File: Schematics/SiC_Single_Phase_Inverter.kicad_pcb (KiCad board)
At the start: 2 copper layers, 200 x 84 mm, 107 parts, among them J1 23AH8785-Black, J2 23AH8786-Red, Q1 STB10NK60ZT4, Q2 STB10NK60ZT4, Q3 C3M0025065K, Q4 C3M0025065K, Q5 C3M0025065K, Q6 C3M0025065K, Q7 C3M0025065K, U1 UCC21710QDWRQ1, U2 UCC21710QDWRQ1, U3 UCC21710QDWRQ1, U4 UCC21710QDWRQ1

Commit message: [WIP SiC Single Phase Inverter
- Updated README.md
- Added New Parts for Output filter L,C,R
- Added datasheets for the new parts
- Added 3D models for the new parts
- Added new symbols and footprints for the L,C,R
- Finished output filter
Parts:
- added C53: 6.8 uF, SiC_Inverter:C4AF9BW4680T3FK, F.Cu at (285.0, 65.0)
- added J3: 23AH8786-Red, SiC_Inverter:23AH8786-Red, F.Cu at (273.3, 74.1)
- added J4: 23AH8785-Black, SiC_Inverter:23AH8785-Black, F.Cu at (273.4, 108.4)
- added L3: 470 uH, SiC_Inverter:1140471KRC, F.Cu at (229.2, 66.4)
- added L4: 470 uH, SiC_Inverter:1140471KRC, F.Cu at (229.2, 107.6)
- added R34: R, SiC_Inverter:CW005100R0JE12HE, F.Cu at (287.6, 78.0)
- moved C1 51.0 mm to (126.6, 84.3)
- moved L2 51.0 mm to (92.0, 70.7)
- moved C12 51.0 mm to (57.4, 53.8)
- moved C13 51.0 mm to (57.4, 64.9)
- moved C14 51.0 mm to (57.4, 76.1)
- moved C15 51.0 mm to (57.4, 87.2)
- moved C16 51.0 mm to (57.4, 98.4)
- moved C17 51.0 mm to (214.4, 79.0)
- moved C18 51.0 mm to (203.7, 102.7)
- moved C19 51.0 mm to (203.7, 105.7)
- moved C2 51.0 mm to (28.9, 55.4)
- moved C20 51.0 mm to (213.4, 102.8)
- moved C21 51.0 mm to (203.7, 108.7)
- moved C22 51.0 mm to (214.4, 82.4)
- moved C23 51.0 mm to (213.4, 106.2)
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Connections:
- net /Input_Protection/Gate_node_Inpro renamed /Input_Protection/Gate_node_input_pro
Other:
- board size 200 x 84 mm -> 318.5 x 84 mm

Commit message: [WIP SiC Single Phase Inverter]
- Added PCB to PCB Male and Female connectors
- Added symbols, footprints and 3d models for the parts listed above
- Added Male and Female connectors to input protection and input emi
  subsheets
- Changed PCB editor to account for two edge cuts/ two sub circuits
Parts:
- removed Q6: C3M0025065K, SiC_Inverter:C3M0025065K
- added J5: 464369202, SiC_Inverter:46436-900_02, F.Cu at (98.3, 42.2)
- added J6: 464379202, SiC_Inverter:46437-900_02, F.Cu at (141.0, 35.0)
- added J7: 464369202, SiC_Inverter:46436-900_02, F.Cu at (237.0, 59.0)
- moved C12 377.7 mm to (434.3, 29.5)
- moved C13 377.7 mm to (434.3, 40.6)
- moved C14 377.7 mm to (434.3, 51.8)
- moved C15 377.7 mm to (434.3, 63.0)
- moved C16 377.7 mm to (434.3, 74.1)
- moved C2 377.7 mm to (405.8, 31.2)
- moved C3 377.7 mm to (405.8, 45.7)
- moved C4 377.7 mm to (405.8, 60.3)
- moved C5 377.7 mm to (405.8, 74.8)
- moved C6 377.7 mm to (405.8, 89.4)
- moved C10 377.7 mm to (420.7, 74.8)
- moved C11 377.7 mm to (420.7, 89.4)
- moved C7 377.7 mm to (420.7, 31.2)
- moved C8 377.7 mm to (420.7, 45.7)
- moved C9 377.7 mm to (420.7, 60.3)
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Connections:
- D1 pad 1: /Input_Protection/Gate_node_input_pro -> GND
- R1 pad 2: /Input_Protection/Gate_node_input_pro -> GND
- R2 pad 2: /Input_Protection/Gate_node_input_pro -> GND
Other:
- board size 318.5 x 84 mm -> 204.5 x 65.2 mm
- board text added: "DC Input and Input Protection Circuit"
- board text added: "EMI Input Filter"

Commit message: [WIP Single Phase SiC Inverter]
- Added molex 4 pin pcb connector for +15V power
- Added 3d model, symbol and footprint
- Added datasheet for molex connector
- Added Male and Female pcb - pcb connectors to all sub sheets
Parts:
- added J10: 464379202, SiC_Inverter:46437-900_02, F.Cu at (397.3, 112.2)
- added J11: 464369202, SiC_Inverter:46436-900_02, F.Cu at (380.2, 112.2)
- added J12: 464379202, SiC_Inverter:46437-900_02, F.Cu at (461.5, 44.5)
- added J13: 464369202, SiC_Inverter:46436-900_02, F.Cu at (461.5, 17.4)
- added J14: 464379202, SiC_Inverter:46437-900_02, F.Cu at (458.6, 111.0)
- added J15: 464369202, SiC_Inverter:46436-900_02, F.Cu at (476.0, 111.0)
- added J16: 464379202, SiC_Inverter:46437-900_02, F.Cu at (349.7, 50.9)
- added J8: 43650-0418, SiC_Inverter:436500418, F.Cu at (356.5, 155.2)
- added J9: 43650-0418, SiC_Inverter:436500418, F.Cu at (467.6, 95.1)
- added PS1: IRM-03-15, SiC_Inverter:IRM-03-15, F.Cu at (323.0, 163.1)
- added PS2: IRM-03-15, SiC_Inverter:IRM-03-15, F.Cu at (323.0, 188.6)
- moved J2 405.5 mm to (435.0, 158.8), turned to 0 degrees
- moved J1 388.3 mm to (421.4, 158.8), turned to 0 degrees
- moved D1 382.4 mm to (423.1, 194.1)
- moved D2 382.4 mm to (416.5, 189.3)
- moved F1 382.4 mm to (432.0, 173.6)
- moved Q1 382.4 mm to (425.3, 180.5)
- moved R1 382.4 mm to (417.5, 193.5)
- moved R2 382.4 mm to (417.5, 196.8)
- moved J5 368.3 mm to (437.4, 186.0), turned to 0 degrees
- moved J6 237.9 mm to (360.9, 125.9), turned to 0 degrees
- moved L2 160.8 mm to (304.8, 112.7)
- moved L1 156.5 mm to (307.3, 131.3)
- moved C1 146.2 mm to (339.6, 102.3)
- moved J7 126.0 mm to (343.8, 125.9), turned to 0 degrees
- moved R3 100.2 mm to (376.9, 95.4)
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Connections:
- C17 pad 2: GND_ISO_LALS -> GND_ISO_LAHS
- C22 pad 1: +15V__ISO_LAHS -> +15V_ISO_LALS
- C26 pad 1: +15V__ISO_LAHS -> +15V_ISO_LALS
- C27 pad 1: +15V__ISO_LAHS -> +15V_ISO_LALS
- C29 pad 2: GND_ISO_LALS -> GND_ISO_LAHS
- C30 pad 2: GND_ISO_LALS -> GND_ISO_LAHS
- C35 pad 1: +15V__ISO_LBHS -> +15V_ISO_LBLS
- C36 pad 2: GND_ISO_LBLS -> GND_ISO_LBHS
- C37 pad 1: +15V__ISO_LBHS -> +15V_ISO_LBLS
- C38 pad 2: GND_ISO_LBLS -> GND_ISO_LBHS
- C39 pad 1: +15V__ISO_LBHS -> +15V_ISO_LBLS
- C40 pad 2: GND_ISO_LBLS -> GND_ISO_LBHS
- D2 pad 1: /Input_Protection/+VIN_Protected -> /EMI_Input_Filter/+VIN_EMI
- D4 pad 2: GND_ISO_LALS -> GND_ISO_LAHS
- D6 pad 2: GND_ISO_LBLS -> GND_ISO_LBHS
- F1 pad 2: /Input_Protection/+VIN_Protected -> /EMI_Input_Filter/+VIN_EMI
- J5 pad P1_1: /Input_Protection/+VIN_Protected -> /EMI_Input_Filter/+VIN_EMI
- J5 pad P1_10: /Input_Protection/+VIN_Protected -> /EMI_Input_Filter/+VIN_EMI
- J5 pad P1_2: /Input_Protection/+VIN_Protected -> /EMI_Input_Filter/+VIN_EMI
- J5 pad P1_3: /Input_Protection/+VIN_Protected -> /EMI_Input_Filter/+VIN_EMI
- J5 pad P1_4: /Input_Protection/+VIN_Protected -> /EMI_Input_Filter/+VIN_EMI
- J5 pad P1_5: /Input_Protection/+VIN_Protected -> /EMI_Input_Filter/+VIN_EMI
- J5 pad P1_6: /Input_Protection/+VIN_Protected -> /EMI_Input_Filter/+VIN_EMI
- J5 pad P1_7: /Input_Protection/+VIN_Protected -> /EMI_Input_Filter/+VIN_EMI
- J5 pad P1_8: /Input_Protection/+VIN_Protected -> /EMI_Input_Filter/+VIN_EMI
- J5 pad P1_9: /Input_Protection/+VIN_Protected -> /EMI_Input_Filter/+VIN_EMI
- Q3 pad 1: /Full-Bridge/BUS_DC+ -> /DC_Link_Caps/BUS_DC+
- Q4 pad 1: /Full-Bridge/BUS_DC+ -> /DC_Link_Caps/BUS_DC+
- Q5 pad 2: GND_ISO_LBLS -> GND_ISO_LBHS
- Q5 pad 3: GND_ISO_LBLS -> GND_ISO_LBHS
- Q7 pad 2: GND_ISO_LALS -> GND_ISO_LAHS
- Q7 pad 3: GND_ISO_LALS -> GND_ISO_LAHS
- R21 pad 2: GND_ISO_LBLS -> GND_ISO_LBHS
- R8 pad 2: GND_ISO_LALS -> GND_ISO_LAHS
- U1 pad 5: +15V__ISO_LAHS -> +15V_ISO_LALS
- U2 pad 1: GND_ISO_LALS -> GND_ISO_LAHS
- U2 pad 2: GND_ISO_LALS -> GND_ISO_LAHS
- U2 pad 3: GND_ISO_LALS -> GND_ISO_LAHS
- U2 pad 8: GND_ISO_LALS -> GND_ISO_LAHS
- U3 pad 1: GND_ISO_LBLS -> GND_ISO_LBHS
- U3 pad 2: GND_ISO_LBLS -> GND_ISO_LBHS
- U3 pad 3: GND_ISO_LBLS -> GND_ISO_LBHS
- U3 pad 8: GND_ISO_LBLS -> GND_ISO_LBHS
- U4 pad 5: +15V__ISO_LBHS -> +15V_ISO_LBLS

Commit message: Updating README
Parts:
- added IC1: F280049CPMSR, SiC_Inverter:F280049CPMSR, F.Cu at (460.3, 181.8)

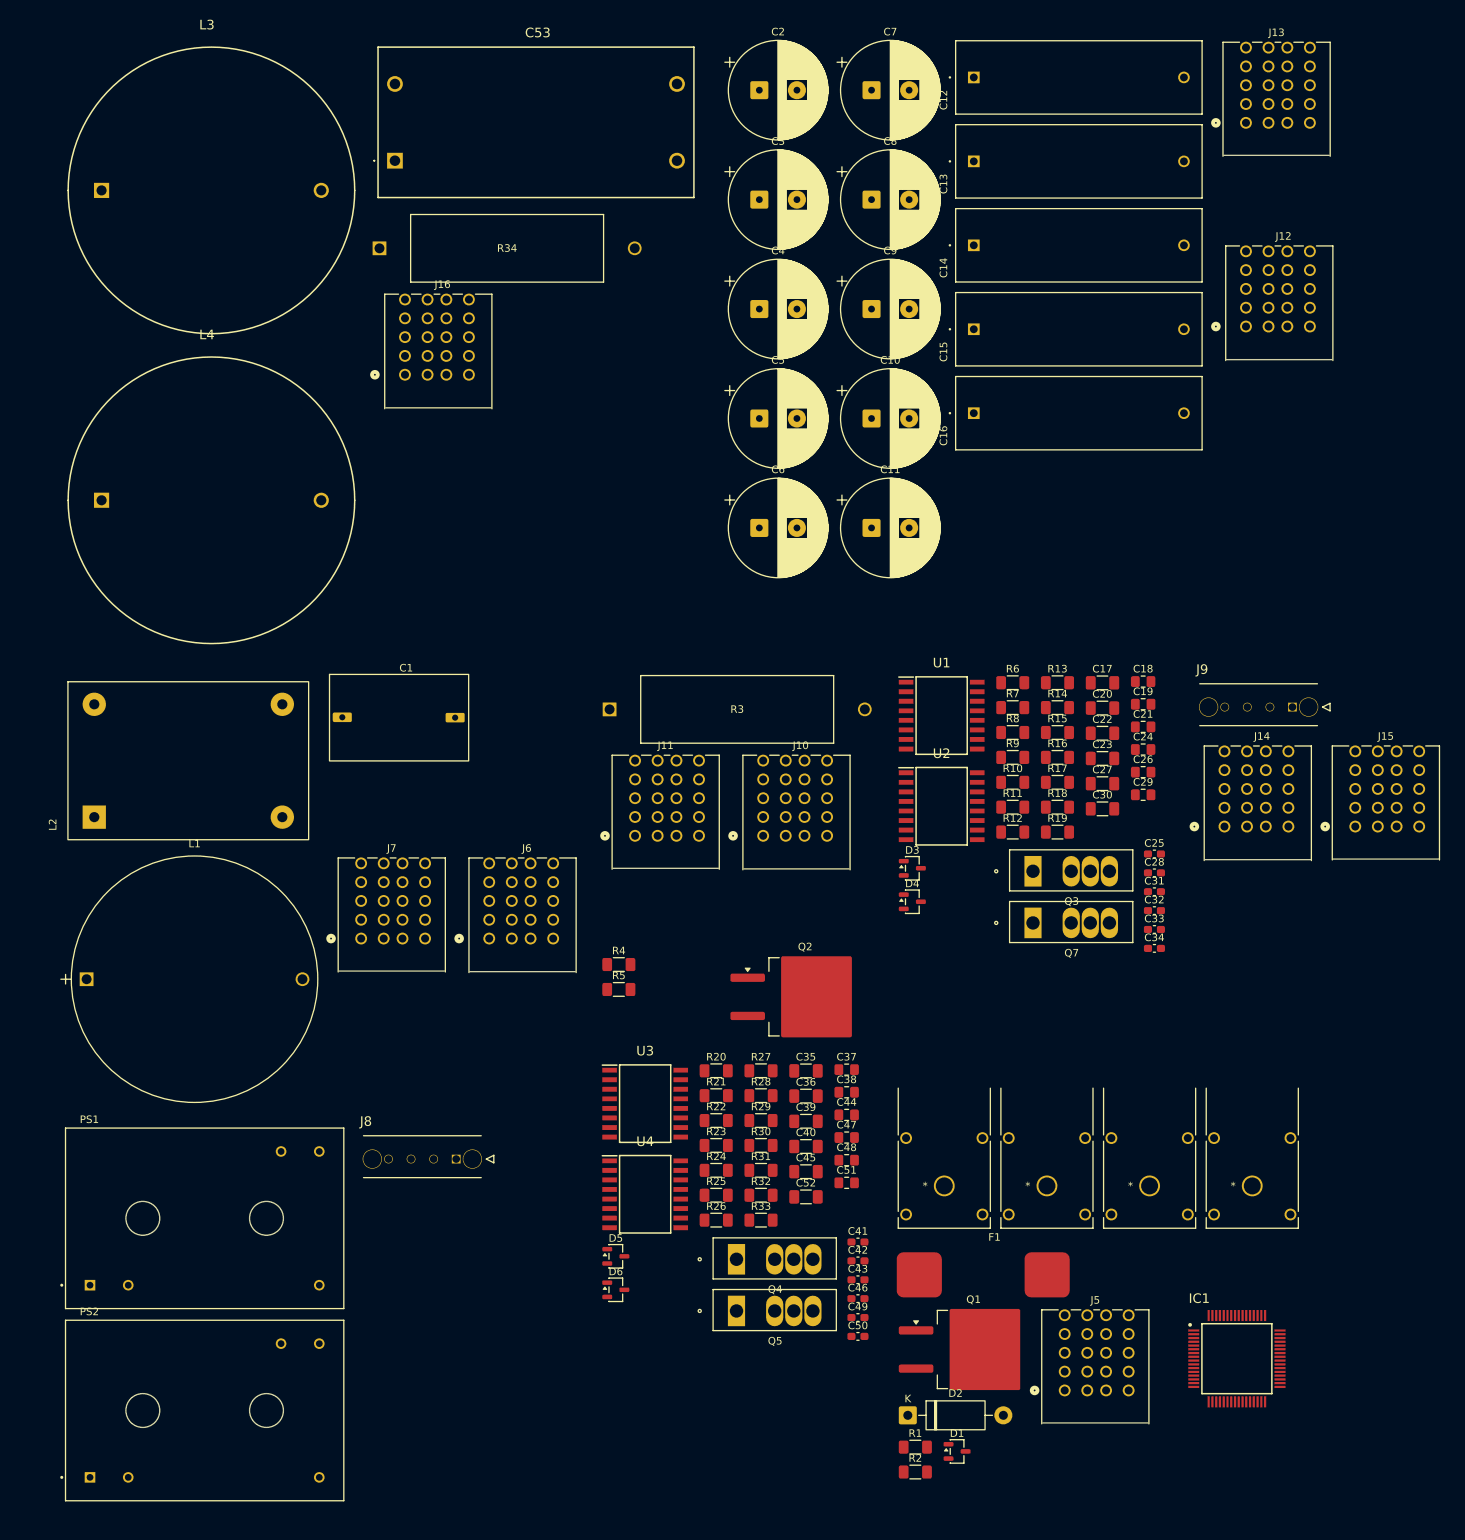
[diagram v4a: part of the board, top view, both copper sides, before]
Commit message: [WIP Single Phase Inverter]
- Changed all Refs within each sub sheet (Stripe)
- Added 3V3 Power Supply off of 15V iso supply
- Added footprint, symbol and 3d part
- updated PCB with new part
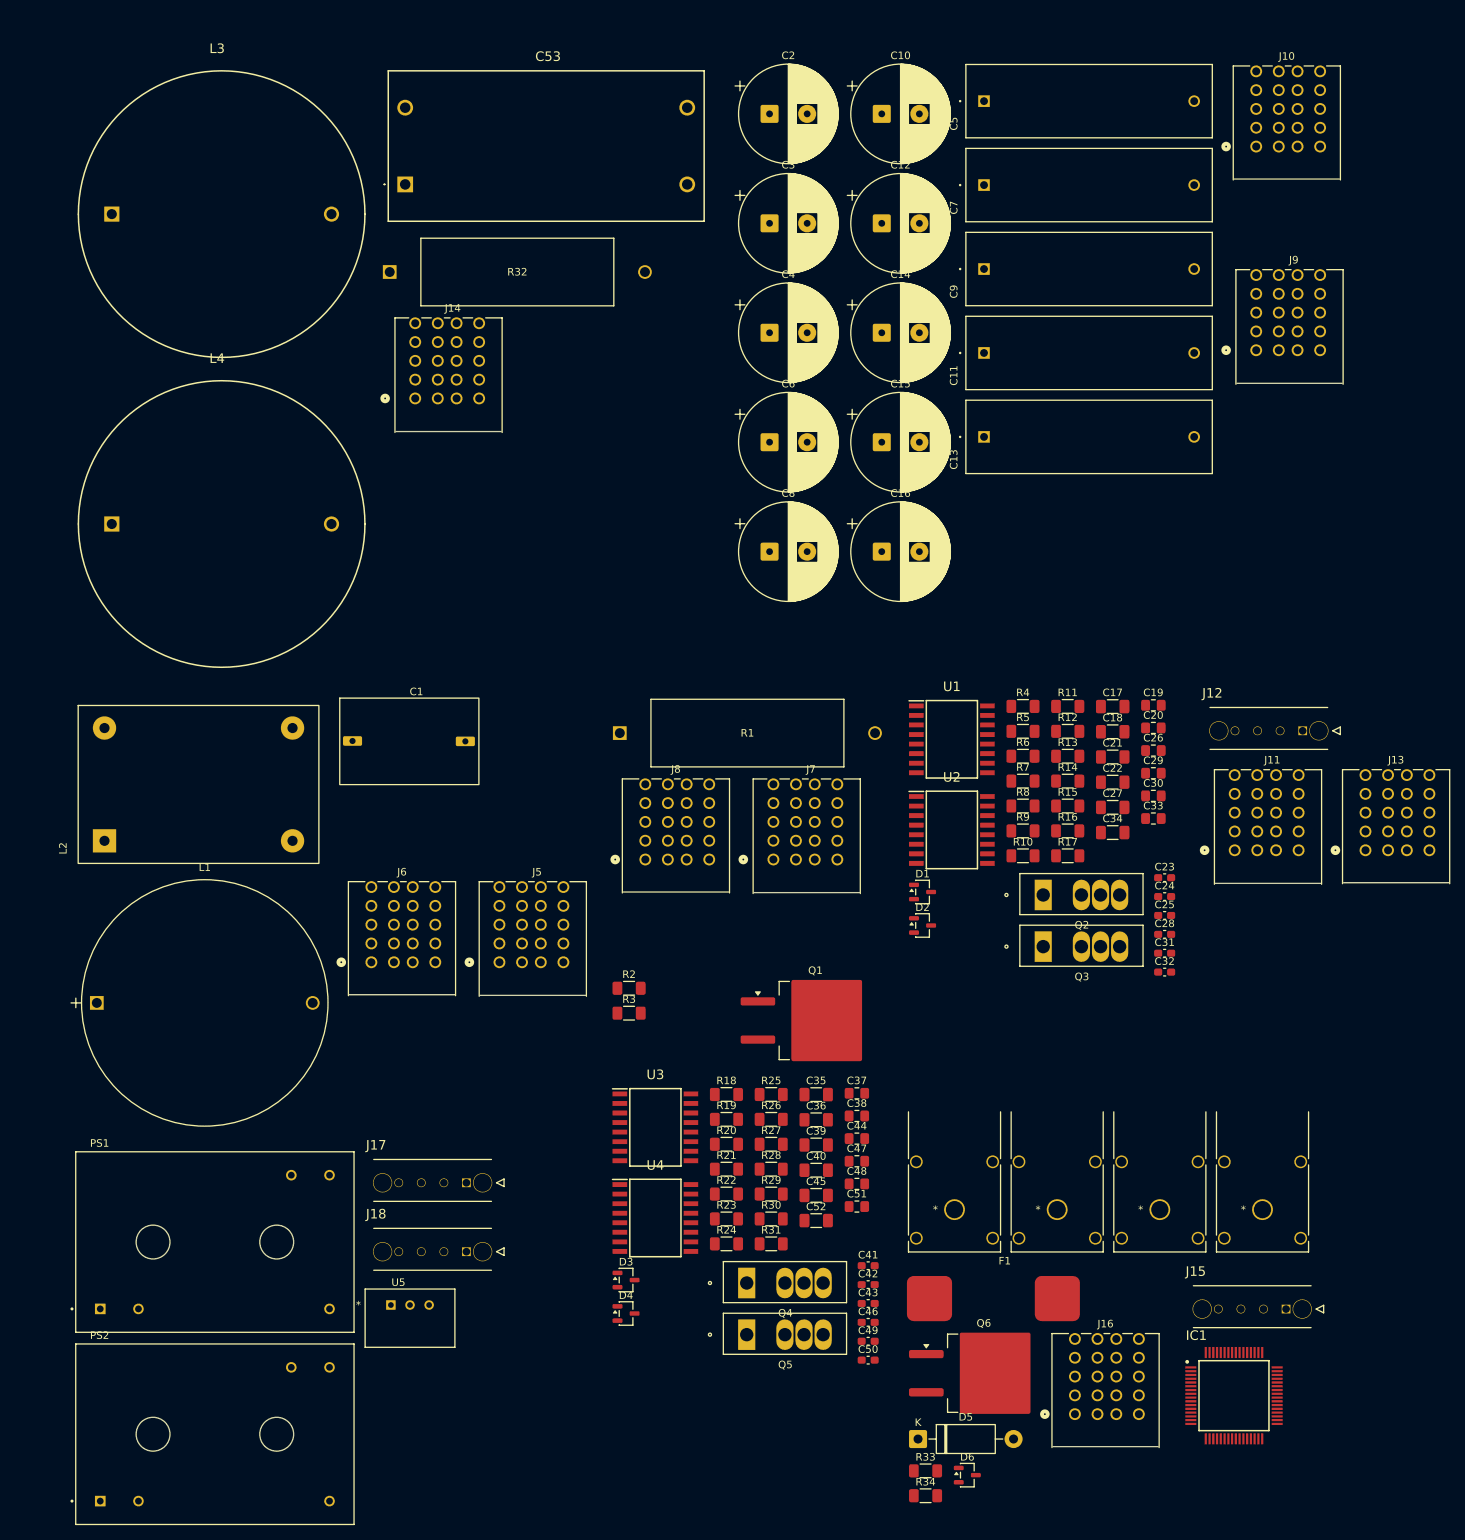
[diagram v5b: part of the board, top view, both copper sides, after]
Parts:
- removed Q7: C3M0025065K, SiC_Inverter:C3M0025065K
- added J17: 43650-0418, SiC_Inverter:436500418, F.Cu at (357.8, 158.4)
- added J18: 43650-0418, SiC_Inverter:436500418, F.Cu at (357.8, 167.5)
- added Q6: STB10NK60ZT4, Package_TO_SOT_SMD:TO-263-2, F.Cu at (426.6, 183.7)
- added U5: TR05S3V3, SiC_Inverter:TR05S3V3, F.Cu at (347.8, 174.6)
- C11, C5, C7, C9: value 22 uF -> 2 uF; footprint SiC_Inverter:ESH226M500AL4AA -> SiC_Inverter:MKP1848C52050JK2
- C12, C14, C15, C16: value 2 uF -> 22 uF; footprint SiC_Inverter:MKP1848C52050JK2 -> SiC_Inverter:ESH226M500AL4AA
- C18: value 0.1 u -> 15 u; footprint Capacitor_SMD:C_0805_2012Metric_Pad1.18x1.45mm_HandSolder -> Capacitor_SMD:C_1206_3216Metric_Pad1.33x1.80mm_HandSolder
- C20, C30: value 1 u -> 0.1 u; footprint Capacitor_SMD:C_1206_3216Metric_Pad1.33x1.80mm_HandSolder -> Capacitor_SMD:C_0805_2012Metric_Pad1.18x1.45mm_HandSolder
- C21: value 0.1 u -> 1 u; footprint Capacitor_SMD:C_0805_2012Metric_Pad1.18x1.45mm_HandSolder -> Capacitor_SMD:C_1206_3216Metric_Pad1.33x1.80mm_HandSolder
- C22: value 15 u -> 1 u
- C23: value 1 u -> 100 p; footprint Capacitor_SMD:C_1206_3216Metric_Pad1.33x1.80mm_HandSolder -> Capacitor_SMD:C_0603_1608Metric_Pad1.08x0.95mm_HandSolder
- C24: value 0.1 u -> 100 p; footprint Capacitor_SMD:C_0805_2012Metric_Pad1.18x1.45mm_HandSolder -> Capacitor_SMD:C_0603_1608Metric_Pad1.08x0.95mm_HandSolder
- C33: value 100 p -> 0.1 u; footprint Capacitor_SMD:C_0603_1608Metric_Pad1.08x0.95mm_HandSolder -> Capacitor_SMD:C_0805_2012Metric_Pad1.18x1.45mm_HandSolder
- C34: value 100 p -> 1 u; footprint Capacitor_SMD:C_0603_1608Metric_Pad1.08x0.95mm_HandSolder -> Capacitor_SMD:C_1206_3216Metric_Pad1.33x1.80mm_HandSolder
- D1: value BZX84C15-7-F -> BZX84C20-7-F
- D2: value P6KE500A-HF -> BZX84C20-7-F; footprint Diode_THT:D_DO-15_P12.70mm_Horizontal -> Package_TO_SOT_SMD:SOT-23-3
- D5: value BZX84C20-7-F -> P6KE500A-HF; footprint Package_TO_SOT_SMD:SOT-23-3 -> Diode_THT:D_DO-15_P12.70mm_Horizontal
- D6: value BZX84C20-7-F -> BZX84C15-7-F
- J1: value 23AH8785-Black -> 23AH8786-Red; footprint SiC_Inverter:23AH8785-Black -> SiC_Inverter:23AH8786-Red
- J10, J16, J6: value 464379202 -> 464369202; footprint SiC_Inverter:46437-900_02 -> SiC_Inverter:46436-900_02
- J11, J5, J7: value 464369202 -> 464379202; footprint SiC_Inverter:46436-900_02 -> SiC_Inverter:46437-900_02
- J12: value 464379202 -> 43650-0418; footprint SiC_Inverter:46437-900_02 -> SiC_Inverter:436500418
- J15: value 464369202 -> 43650-0418; footprint SiC_Inverter:46436-900_02 -> SiC_Inverter:436500418
- J2: value 23AH8786-Red -> 23AH8785-Black; footprint SiC_Inverter:23AH8786-Red -> SiC_Inverter:23AH8785-Black
- J8: value 43650-0418 -> 464369202; footprint SiC_Inverter:436500418 -> SiC_Inverter:46436-900_02
- J9: value 43650-0418 -> 464379202; footprint SiC_Inverter:436500418 -> SiC_Inverter:46437-900_02
- Q2: value STB10NK60ZT4 -> C3M0025065K; footprint Package_TO_SOT_SMD:TO-263-2 -> SiC_Inverter:C3M0025065K
- R1: value 100K -> CW005100R0JE12HE; footprint Resistor_SMD:R_1206_3216Metric_Pad1.30x1.75mm_HandSolder -> SiC_Inverter:CW005100R0JE12HE
- R13: value 100K -> 5K
- R14, R25: value 10 -> 100
- R15, R24: value 10 -> 5K
- R18, R19: value 5K -> 100K
- R20, R21, R8: value 100K -> 10
- R27, R30: value 100 -> 5K
- R28: value 5K -> 100
- R3: value CW005100R0JE12HE -> 100K; footprint SiC_Inverter:CW005100R0JE12HE -> Resistor_SMD:R_1206_3216Metric_Pad1.30x1.75mm_HandSolder
- R32: value 5K -> R; footprint Resistor_SMD:R_1206_3216Metric_Pad1.30x1.75mm_HandSolder -> SiC_Inverter:CW005100R0JE12HE
- R33: value 5K -> 47
- R34: value R -> 100K; footprint SiC_Inverter:CW005100R0JE12HE -> Resistor_SMD:R_1206_3216Metric_Pad1.30x1.75mm_HandSolder
- R4: value 47 -> 100K
- R9: value 100 -> 10
- moved R34 181.0 mm to (418.9, 200.0)
- moved J16 164.4 mm to (438.7, 189.1)
- moved R32 132.3 mm to (347.6, 37.3)
- moved J14 121.7 mm to (351.0, 54.1)
- moved J10 112.7 mm to (462.8, 20.6)
- moved R1 102.7 mm to (378.2, 98.6)
- moved J13 98.0 mm to (477.4, 114.2)
- moved J5 94.3 mm to (362.2, 129.0)
- moved J11 79.7 mm to (460.0, 114.2)
- moved R2 74.7 mm to (379.4, 132.5)
- moved D1 74.5 mm to (418.5, 119.7)
- moved D4 66.7 mm to (379.1, 175.7)
- moved D3 66.7 mm to (379.1, 171.3)
- moved D2 65.2 mm to (418.5, 124.2)
- moved J15 64.8 mm to (466.8, 175.2)
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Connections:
- C18 pad 1: +3V3 -> +15V_ISO_LALS
- C18 pad 2: LOGIC_GND -> GND_ISO_LAHS
- C19 pad 1: +3V3 -> +15V_ISO_LALS
- C19 pad 2: LOGIC_GND -> GND_ISO_LAHS
- C20 pad 1: +3V3 -> +15V_ISO_LALS
- C20 pad 2: LOGIC_GND -> GND_ISO_LAHS
- C21 pad 1: Net-(U1-IN+) -> +15V_ISO_LALS
- C21 pad 2: LOGIC_GND -> GND_ISO_LAHS
- C23 pad 1: +3V3 -> /Full-Bridge/LS_LegA_RDY
- C24 pad 1: Net-(U2-IN+) -> /Full-Bridge/~{LS_LegA_FLT}
- C25 pad 1: /Full-Bridge/HS_LegA_EN -> /Full-Bridge/LS_LegA_EN
- C26 pad 1: +15V_ISO_LALS -> +3V3
- C26 pad 2: GND_ISO_LAHS -> LOGIC_GND
- C27 pad 1: +15V_ISO_LALS -> +3V3
- C27 pad 2: GND_ISO_LAHS -> LOGIC_GND
- C28 pad 1: /Full-Bridge/~{HS_LegA_FLT} -> /Full-Bridge/HS_LegA_RDY
- C29 pad 1: +15V_ISO_LALS -> Net-(U1-IN+)
- C29 pad 2: GND_ISO_LAHS -> LOGIC_GND
- C30 pad 1: +15V_ISO_LALS -> Net-(U2-IN+)
- C30 pad 2: GND_ISO_LAHS -> LOGIC_GND
- C31 pad 1: /Full-Bridge/HS_LegA_RDY -> /Full-Bridge/~{HS_LegA_FLT}
- C32 pad 1: /Full-Bridge/LS_LegA_RDY -> /Full-Bridge/HS_LegA_EN
- C33 pad 1: /Full-Bridge/~{LS_LegA_FLT} -> +3V3
- C34 pad 1: /Full-Bridge/LS_LegA_EN -> +3V3
- D1 pad 1: GND -> /Full-Bridge/Leg_A_Power_Stage/LegA_HS_Gate
- D1 pad 2: GND -> GND_ISO_LAHS
- D2 pad 1: /EMI_Input_Filter/+VIN_EMI -> /Full-Bridge/Leg_A_Power_Stage/LegA_LS_Gate
- D2 pad 2: GND -> GND_ISO_LAHS
- D3 pad 1: /Full-Bridge/Leg_A_Power_Stage/LegA_HS_Gate -> /Full-Bridge/Leg_B_Power_Stage/LegB_HS_Gate
- D3 pad 2: GND_ISO_LAHS -> GND_ISO_LBHS
- D4 pad 1: /Full-Bridge/Leg_A_Power_Stage/LegA_LS_Gate -> /Full-Bridge/Leg_B_Power_Stage/LegB_LS_Gate
- D4 pad 2: GND_ISO_LAHS -> GND_ISO_LBHS
- D5 pad 1: /Full-Bridge/Leg_B_Power_Stage/LegB_HS_Gate -> /EMI_Input_Filter/+VIN_EMI
- D5 pad 2: GND_ISO_LBHS -> GND
- D6 pad 1: /Full-Bridge/Leg_B_Power_Stage/LegB_LS_Gate -> GND
- D6 pad 2: GND_ISO_LBHS -> GND
- J1 pad 1: -VIN -> +VIN
- J10 pad P1_1: GND -> /DC_Link_Caps/BUS_DC+
- J10 pad P1_10: GND -> /DC_Link_Caps/BUS_DC+
- J10 pad P1_2: GND -> /DC_Link_Caps/BUS_DC+
- J10 pad P1_3: GND -> /DC_Link_Caps/BUS_DC+
- J10 pad P1_4: GND -> /DC_Link_Caps/BUS_DC+
- J10 pad P1_5: GND -> /DC_Link_Caps/BUS_DC+
- J10 pad P1_6: GND -> /DC_Link_Caps/BUS_DC+
- J10 pad P1_7: GND -> /DC_Link_Caps/BUS_DC+
- J10 pad P1_8: GND -> /DC_Link_Caps/BUS_DC+
- J10 pad P1_9: GND -> /DC_Link_Caps/BUS_DC+
- J10 pad P2_1: /EMI_Input_Filter/BUS+_Filtered -> GND
- J10 pad P2_10: /EMI_Input_Filter/BUS+_Filtered -> GND
- J10 pad P2_2: /EMI_Input_Filter/BUS+_Filtered -> GND
- J10 pad P2_3: /EMI_Input_Filter/BUS+_Filtered -> GND
- J10 pad P2_4: /EMI_Input_Filter/BUS+_Filtered -> GND
- J10 pad P2_5: /EMI_Input_Filter/BUS+_Filtered -> GND
- J10 pad P2_6: /EMI_Input_Filter/BUS+_Filtered -> GND
- J10 pad P2_7: /EMI_Input_Filter/BUS+_Filtered -> GND
- J10 pad P2_8: /EMI_Input_Filter/BUS+_Filtered -> GND
- J10 pad P2_9: /EMI_Input_Filter/BUS+_Filtered -> GND
- J11 pad P1_1: /DC_Link_Caps/BUS_DC+ -> GND
- J11 pad P1_10: /DC_Link_Caps/BUS_DC+ -> GND
- J11 pad P1_2: /DC_Link_Caps/BUS_DC+ -> GND
- J11 pad P1_3: /DC_Link_Caps/BUS_DC+ -> GND
- J11 pad P1_4: /DC_Link_Caps/BUS_DC+ -> GND
- J11 pad P1_5: /DC_Link_Caps/BUS_DC+ -> GND
- J11 pad P1_6: /DC_Link_Caps/BUS_DC+ -> GND
- J11 pad P1_7: /DC_Link_Caps/BUS_DC+ -> GND
- J11 pad P1_8: /DC_Link_Caps/BUS_DC+ -> GND
- J11 pad P1_9: /DC_Link_Caps/BUS_DC+ -> GND
- J11 pad P2_1: GND -> /DC_Link_Caps/BUS_DC+
- J11 pad P2_10: GND -> /DC_Link_Caps/BUS_DC+
- J11 pad P2_2: GND -> /DC_Link_Caps/BUS_DC+
- J11 pad P2_3: GND -> /DC_Link_Caps/BUS_DC+
- J11 pad P2_4: GND -> /DC_Link_Caps/BUS_DC+
- J11 pad P2_5: GND -> /DC_Link_Caps/BUS_DC+
- J11 pad P2_6: GND -> /DC_Link_Caps/BUS_DC+
- J11 pad P2_7: GND -> /DC_Link_Caps/BUS_DC+
- J11 pad P2_8: GND -> /DC_Link_Caps/BUS_DC+
- J11 pad P2_9: GND -> /DC_Link_Caps/BUS_DC+
- J13 pad P1_1: /DC_Link_Caps/BUS_DC+ -> GND_ISO_LAHS
- J13 pad P1_10: /DC_Link_Caps/BUS_DC+ -> GND_ISO_LAHS
- J13 pad P1_2: /DC_Link_Caps/BUS_DC+ -> GND_ISO_LAHS
- J13 pad P1_3: /DC_Link_Caps/BUS_DC+ -> GND_ISO_LAHS
- J13 pad P1_4: /DC_Link_Caps/BUS_DC+ -> GND_ISO_LAHS
- J13 pad P1_5: /DC_Link_Caps/BUS_DC+ -> GND_ISO_LAHS
- J13 pad P1_6: /DC_Link_Caps/BUS_DC+ -> GND_ISO_LAHS
- J13 pad P1_7: /DC_Link_Caps/BUS_DC+ -> GND_ISO_LAHS
- J13 pad P1_8: /DC_Link_Caps/BUS_DC+ -> GND_ISO_LAHS
- J13 pad P1_9: /DC_Link_Caps/BUS_DC+ -> GND_ISO_LAHS
- J13 pad P2_1: GND -> GND_ISO_LBHS
- J13 pad P2_10: GND -> GND_ISO_LBHS
- J13 pad P2_2: GND -> GND_ISO_LBHS
- J13 pad P2_3: GND -> GND_ISO_LBHS
- J13 pad P2_4: GND -> GND_ISO_LBHS
- J13 pad P2_5: GND -> GND_ISO_LBHS
- J13 pad P2_6: GND -> GND_ISO_LBHS
- J13 pad P2_7: GND -> GND_ISO_LBHS
- J13 pad P2_8: GND -> GND_ISO_LBHS
- J13 pad P2_9: GND -> GND_ISO_LBHS
- J14 pad P1_1: GND -> GND_ISO_LBHS
- J14 pad P1_10: GND -> GND_ISO_LBHS
- J14 pad P1_2: GND -> GND_ISO_LBHS
- J14 pad P1_3: GND -> GND_ISO_LBHS
- J14 pad P1_4: GND -> GND_ISO_LBHS
- J14 pad P1_5: GND -> GND_ISO_LBHS
- J14 pad P1_6: GND -> GND_ISO_LBHS
- J14 pad P1_7: GND -> GND_ISO_LBHS
- J14 pad P1_8: GND -> GND_ISO_LBHS
- J14 pad P1_9: GND -> GND_ISO_LBHS
- J14 pad P2_1: /DC_Link_Caps/BUS_DC+ -> GND_ISO_LAHS
- J14 pad P2_10: /DC_Link_Caps/BUS_DC+ -> GND_ISO_LAHS
- J14 pad P2_2: /DC_Link_Caps/BUS_DC+ -> GND_ISO_LAHS
- J14 pad P2_3: /DC_Link_Caps/BUS_DC+ -> GND_ISO_LAHS
- J14 pad P2_4: /DC_Link_Caps/BUS_DC+ -> GND_ISO_LAHS
- J14 pad P2_5: /DC_Link_Caps/BUS_DC+ -> GND_ISO_LAHS
- J14 pad P2_6: /DC_Link_Caps/BUS_DC+ -> GND_ISO_LAHS
- J14 pad P2_7: /DC_Link_Caps/BUS_DC+ -> GND_ISO_LAHS
- J14 pad P2_8: /DC_Link_Caps/BUS_DC+ -> GND_ISO_LAHS
- J14 pad P2_9: /DC_Link_Caps/BUS_DC+ -> GND_ISO_LAHS
- J16 pad P1_1: GND_ISO_LBHS -> /EMI_Input_Filter/+VIN_EMI
- J16 pad P1_10: GND_ISO_LBHS -> /EMI_Input_Filter/+VIN_EMI
- J16 pad P1_2: GND_ISO_LBHS -> /EMI_Input_Filter/+VIN_EMI
- J16 pad P1_3: GND_ISO_LBHS -> /EMI_Input_Filter/+VIN_EMI
- J16 pad P1_4: GND_ISO_LBHS -> /EMI_Input_Filter/+VIN_EMI
- J16 pad P1_5: GND_ISO_LBHS -> /EMI_Input_Filter/+VIN_EMI
- J16 pad P1_6: GND_ISO_LBHS -> /EMI_Input_Filter/+VIN_EMI
- J16 pad P1_7: GND_ISO_LBHS -> /EMI_Input_Filter/+VIN_EMI
- J16 pad P1_8: GND_ISO_LBHS -> /EMI_Input_Filter/+VIN_EMI
- J16 pad P1_9: GND_ISO_LBHS -> /EMI_Input_Filter/+VIN_EMI
- J16 pad P2_1: GND_ISO_LAHS -> GND
- J16 pad P2_10: GND_ISO_LAHS -> GND
- J16 pad P2_2: GND_ISO_LAHS -> GND
- J16 pad P2_3: GND_ISO_LAHS -> GND
- J16 pad P2_4: GND_ISO_LAHS -> GND
- J16 pad P2_5: GND_ISO_LAHS -> GND
- J16 pad P2_6: GND_ISO_LAHS -> GND
- J16 pad P2_7: GND_ISO_LAHS -> GND
- J16 pad P2_8: GND_ISO_LAHS -> GND
- J16 pad P2_9: GND_ISO_LAHS -> GND
- J2 pad 1: +VIN -> -VIN
- J5 pad P1_1: /EMI_Input_Filter/+VIN_EMI -> GND
- J5 pad P1_10: /EMI_Input_Filter/+VIN_EMI -> GND
- J5 pad P1_2: /EMI_Input_Filter/+VIN_EMI -> GND
- J5 pad P1_3: /EMI_Input_Filter/+VIN_EMI -> GND
- J5 pad P1_4: /EMI_Input_Filter/+VIN_EMI -> GND
- J5 pad P1_5: /EMI_Input_Filter/+VIN_EMI -> GND
- J5 pad P1_6: /EMI_Input_Filter/+VIN_EMI -> GND
- J5 pad P1_7: /EMI_Input_Filter/+VIN_EMI -> GND
- J5 pad P1_8: /EMI_Input_Filter/+VIN_EMI -> GND
- J5 pad P1_9: /EMI_Input_Filter/+VIN_EMI -> GND
- J5 pad P2_1: GND -> /EMI_Input_Filter/+VIN_EMI
- J5 pad P2_10: GND -> /EMI_Input_Filter/+VIN_EMI
- J5 pad P2_2: GND -> /EMI_Input_Filter/+VIN_EMI
- J5 pad P2_3: GND -> /EMI_Input_Filter/+VIN_EMI
- J5 pad P2_4: GND -> /EMI_Input_Filter/+VIN_EMI
- J5 pad P2_5: GND -> /EMI_Input_Filter/+VIN_EMI
- J5 pad P2_6: GND -> /EMI_Input_Filter/+VIN_EMI
- J5 pad P2_7: GND -> /EMI_Input_Filter/+VIN_EMI
- J5 pad P2_8: GND -> /EMI_Input_Filter/+VIN_EMI
- J5 pad P2_9: GND -> /EMI_Input_Filter/+VIN_EMI
- J6 pad P1_1: GND -> /EMI_Input_Filter/BUS+_Filtered
- J6 pad P1_10: GND -> /EMI_Input_Filter/BUS+_Filtered
- J6 pad P1_2: GND -> /EMI_Input_Filter/BUS+_Filtered
- J6 pad P1_3: GND -> /EMI_Input_Filter/BUS+_Filtered
- J6 pad P1_4: GND -> /EMI_Input_Filter/BUS+_Filtered
- J6 pad P1_5: GND -> /EMI_Input_Filter/BUS+_Filtered
- J6 pad P1_6: GND -> /EMI_Input_Filter/BUS+_Filtered
- J6 pad P1_7: GND -> /EMI_Input_Filter/BUS+_Filtered
- J6 pad P1_8: GND -> /EMI_Input_Filter/BUS+_Filtered
- J6 pad P1_9: GND -> /EMI_Input_Filter/BUS+_Filtered
- J6 pad P2_1: /EMI_Input_Filter/+VIN_EMI -> GND
- J6 pad P2_10: /EMI_Input_Filter/+VIN_EMI -> GND
- J6 pad P2_2: /EMI_Input_Filter/+VIN_EMI -> GND
- J6 pad P2_3: /EMI_Input_Filter/+VIN_EMI -> GND
- J6 pad P2_4: /EMI_Input_Filter/+VIN_EMI -> GND
- J6 pad P2_5: /EMI_Input_Filter/+VIN_EMI -> GND
- J6 pad P2_6: /EMI_Input_Filter/+VIN_EMI -> GND
- J6 pad P2_7: /EMI_Input_Filter/+VIN_EMI -> GND
- J6 pad P2_8: /EMI_Input_Filter/+VIN_EMI -> GND
- J6 pad P2_9: /EMI_Input_Filter/+VIN_EMI -> GND
- J7 pad P1_1: /EMI_Input_Filter/BUS+_Filtered -> GND
- J7 pad P1_10: /EMI_Input_Filter/BUS+_Filtered -> GND
- J7 pad P1_2: /EMI_Input_Filter/BUS+_Filtered -> GND
- J7 pad P1_3: /EMI_Input_Filter/BUS+_Filtered -> GND
- J7 pad P1_4: /EMI_Input_Filter/BUS+_Filtered -> GND
- J7 pad P1_5: /EMI_Input_Filter/BUS+_Filtered -> GND
- J7 pad P1_6: /EMI_Input_Filter/BUS+_Filtered -> GND
- J7 pad P1_7: /EMI_Input_Filter/BUS+_Filtered -> GND
- J7 pad P1_8: /EMI_Input_Filter/BUS+_Filtered -> GND
- J7 pad P1_9: /EMI_Input_Filter/BUS+_Filtered -> GND
- J7 pad P2_1: GND -> /EMI_Input_Filter/BUS+_Filtered
- J7 pad P2_10: GND -> /EMI_Input_Filter/BUS+_Filtered
- J7 pad P2_2: GND -> /EMI_Input_Filter/BUS+_Filtered
- J7 pad P2_3: GND -> /EMI_Input_Filter/BUS+_Filtered
- J7 pad P2_4: GND -> /EMI_Input_Filter/BUS+_Filtered
- J7 pad P2_5: GND -> /EMI_Input_Filter/BUS+_Filtered
- J7 pad P2_6: GND -> /EMI_Input_Filter/BUS+_Filtered
- J7 pad P2_7: GND -> /EMI_Input_Filter/BUS+_Filtered
- J7 pad P2_8: GND -> /EMI_Input_Filter/BUS+_Filtered
- J7 pad P2_9: GND -> /EMI_Input_Filter/BUS+_Filtered
- PS2 pad 16: +15V_ISO_LBLS -> +15V_ISO_LALS
- Q1 pad 2: -VIN -> /EMI_Input_Filter/BUS+_Filtered
- Q1 pad 3: GND -> /DC_Link_Caps/BUS_DC+
- Q2 pad 1: Net-(Q2-G) -> /DC_Link_Caps/BUS_DC+
- Q2 pad 2: /EMI_Input_Filter/BUS+_Filtered -> GND_ISO_LAHS
- Q2 pad 3: /DC_Link_Caps/BUS_DC+ -> GND_ISO_LAHS
- Q3 pad 1: /DC_Link_Caps/BUS_DC+ -> GND_ISO_LAHS
- Q3 pad 4: /Full-Bridge/Leg_A_Power_Stage/LegA_HS_Gate -> /Full-Bridge/Leg_A_Power_Stage/LegA_LS_Gate
- R1 pad 1: GND -> /EMI_Input_Filter/BUS+_Filtered
- R1 pad 2: GND -> /DC_Link_Caps/BUS_DC+
- R11 pad 1: Net-(U2-IN+) -> Net-(U1-IN+)
- R13 pad 1: /Full-Bridge/Leg_A_Power_Stage/LegA_HS_Gate -> +3V3
- R13 pad 2: GND_ISO_LAHS -> /Full-Bridge/~{LS_LegA_FLT}
- R14 pad 1: /Full-Bridge/Leg_A_Power_Stage/LegA_LS_OUTL -> Net-(U2-IN+)
- R14 pad 2: /Full-Bridge/Leg_A_Power_Stage/LegA_LS_Gate -> /Full-Bridge/PWM_A_H
- R15 pad 1: /Full-Bridge/Leg_A_Power_Stage/LegA_LS_OUTH -> +3V3
- R15 pad 2: /Full-Bridge/Leg_A_Power_Stage/LegA_LS_Gate -> /Full-Bridge/~{HS_LegA_FLT}
- R16 pad 2: /Full-Bridge/HS_LegA_RDY -> /Full-Bridge/LS_LegA_RDY
- R17 pad 2: /Full-Bridge/~{HS_LegA_FLT} -> /Full-Bridge/HS_LegA_RDY
- R18 pad 1: +3V3 -> /Full-Bridge/Leg_B_Power_Stage/LegB_HS_Gate
- R18 pad 2: /Full-Bridge/~{LS_LegA_FLT} -> GND_ISO_LBHS
- R19 pad 1: +3V3 -> /Full-Bridge/Leg_B_Power_Stage/LegB_LS_Gate
- R19 pad 2: /Full-Bridge/LS_LegA_RDY -> GND_ISO_LBHS
- R2 pad 2: GND -> /Pre-Chrage_current_Limiting/Gate_node_prech
- R20 pad 1: /Full-Bridge/Leg_B_Power_Stage/LegB_HS_Gate -> /Full-Bridge/Leg_B_Power_Stage/LegB_HS_OUTH
- R20 pad 2: GND_ISO_LBHS -> /Full-Bridge/Leg_B_Power_Stage/LegB_HS_Gate
- R21 pad 1: /Full-Bridge/Leg_B_Power_Stage/LegB_LS_Gate -> /Full-Bridge/Leg_B_Power_Stage/LegB_HS_OUTL
- R21 pad 2: GND_ISO_LBHS -> /Full-Bridge/Leg_B_Power_Stage/LegB_HS_Gate
- R22 pad 1: /Full-Bridge/Leg_B_Power_Stage/LegB_HS_OUTH -> /Full-Bridge/Leg_B_Power_Stage/LegB_LS_OUTH
- R22 pad 2: /Full-Bridge/Leg_B_Power_Stage/LegB_HS_Gate -> /Full-Bridge/Leg_B_Power_Stage/LegB_LS_Gate
- R23 pad 1: /Full-Bridge/Leg_B_Power_Stage/LegB_HS_OUTL -> /Full-Bridge/Leg_B_Power_Stage/LegB_LS_OUTL
- R23 pad 2: /Full-Bridge/Leg_B_Power_Stage/LegB_HS_Gate -> /Full-Bridge/Leg_B_Power_Stage/LegB_LS_Gate
- R24 pad 1: /Full-Bridge/Leg_B_Power_Stage/LegB_LS_OUTH -> +3V3
- R24 pad 2: /Full-Bridge/Leg_B_Power_Stage/LegB_LS_Gate -> /Full-Bridge/LS_LegB_EN
- R25 pad 1: /Full-Bridge/Leg_B_Power_Stage/LegB_LS_OUTL -> Net-(U3-IN+)
- R25 pad 2: /Full-Bridge/Leg_B_Power_Stage/LegB_LS_Gate -> /Full-Bridge/PWM_B_L
- R26 pad 2: /Full-Bridge/LS_LegB_EN -> /Full-Bridge/HS_LegB_EN
- R27 pad 1: Net-(U3-IN+) -> +3V3
- R27 pad 2: /Full-Bridge/PWM_B_L -> /Full-Bridge/~{LS_LegB_FLT}
- R28 pad 1: +3V3 -> Net-(U4-IN+)
- R28 pad 2: /Full-Bridge/HS_LegB_EN -> /Full-Bridge/PWM_B_H
- R29 pad 2: /Full-Bridge/~{LS_LegB_FLT} -> /Full-Bridge/~{HS_LegB_FLT}
- R3 pad 1: /EMI_Input_Filter/BUS+_Filtered -> /DC_Link_Caps/BUS_DC+
- R3 pad 2: /DC_Link_Caps/BUS_DC+ -> Net-(Q1-G)
- R30 pad 1: Net-(U4-IN+) -> +3V3
- R30 pad 2: /Full-Bridge/PWM_B_H -> /Full-Bridge/LS_LegB_RDY
- R31 pad 2: /Full-Bridge/~{HS_LegB_FLT} -> /Full-Bridge/HS_LegB_RDY
- R32 pad 1: +3V3 -> /Phase_A_Output
- R32 pad 2: /Full-Bridge/LS_LegB_RDY -> /Phase_B_Output
- R33 pad 1: +3V3 -> Net-(Q6-G)
- R33 pad 2: /Full-Bridge/HS_LegB_RDY -> GND
- R34 pad 1: /Phase_A_Output -> GND
- R34 pad 2: /Phase_B_Output -> GND
- R4 pad 1: Net-(Q2-G) -> /Full-Bridge/Leg_A_Power_Stage/LegA_HS_Gate
- R4 pad 2: /Pre-Chrage_current_Limiting/Gate_node_prech -> GND_ISO_LAHS
- R5 pad 1: /DC_Link_Caps/BUS_DC+ -> /Full-Bridge/Leg_A_Power_Stage/LegA_LS_Gate
- R5 pad 2: Net-(Q2-G) -> GND_ISO_LAHS
- R8 pad 1: /Full-Bridge/Leg_A_Power_Stage/LegA_LS_Gate -> /Full-Bridge/Leg_A_Power_Stage/LegA_LS_OUTH
- R8 pad 2: GND_ISO_LAHS -> /Full-Bridge/Leg_A_Power_Stage/LegA_LS_Gate
- R9 pad 1: Net-(U1-IN+) -> /Full-Bridge/Leg_A_Power_Stage/LegA_LS_OUTL
- R9 pad 2: /Full-Bridge/PWM_A_H -> /Full-Bridge/Leg_A_Power_Stage/LegA_LS_Gate
- U1 pad 12: /Full-Bridge/HS_LegA_RDY -> /Full-Bridge/LS_LegA_RDY
- U1 pad 13: /Full-Bridge/~{HS_LegA_FLT} -> /Full-Bridge/~{LS_LegA_FLT}
- U1 pad 14: /Full-Bridge/HS_LegA_EN -> /Full-Bridge/LS_LegA_EN
- U1 pad 4: /Full-Bridge/Leg_A_Power_Stage/LegA_HS_OUTH -> /Full-Bridge/Leg_A_Power_Stage/LegA_LS_OUTH
- U1 pad 6: /Full-Bridge/Leg_A_Power_Stage/LegA_HS_OUTL -> /Full-Bridge/Leg_A_Power_Stage/LegA_LS_OUTL
- U1 pad 7: /Full-Bridge/Leg_A_Power_Stage/LegA_HS_Gate -> /Full-Bridge/Leg_A_Power_Stage/LegA_LS_Gate
- U2 pad 12: /Full-Bridge/LS_LegA_RDY -> /Full-Bridge/HS_LegA_RDY
- U2 pad 13: /Full-Bridge/~{LS_LegA_FLT} -> /Full-Bridge/~{HS_LegA_FLT}
- U2 pad 14: /Full-Bridge/LS_LegA_EN -> /Full-Bridge/HS_LegA_EN
- U2 pad 4: /Full-Bridge/Leg_A_Power_Stage/LegA_LS_OUTH -> /Full-Bridge/Leg_A_Power_Stage/LegA_HS_OUTH
- U2 pad 6: /Full-Bridge/Leg_A_Power_Stage/LegA_LS_OUTL -> /Full-Bridge/Leg_A_Power_Stage/LegA_HS_OUTL
- U2 pad 7: /Full-Bridge/Leg_A_Power_Stage/LegA_LS_Gate -> /Full-Bridge/Leg_A_Power_Stage/LegA_HS_Gate
